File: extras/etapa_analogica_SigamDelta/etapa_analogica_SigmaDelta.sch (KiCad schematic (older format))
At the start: 19 parts, among them P1 CONN_02X10, P2 CONN_01X03, P3 CONN_02X10, P4 BNC

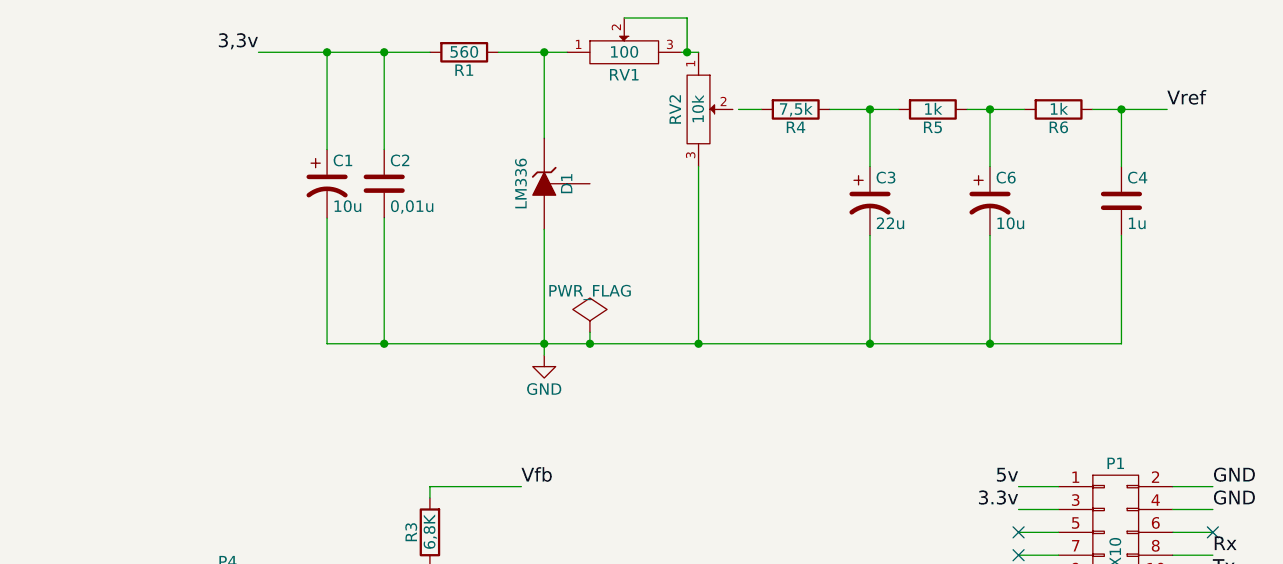
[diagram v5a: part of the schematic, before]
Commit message: choque en filtro vref
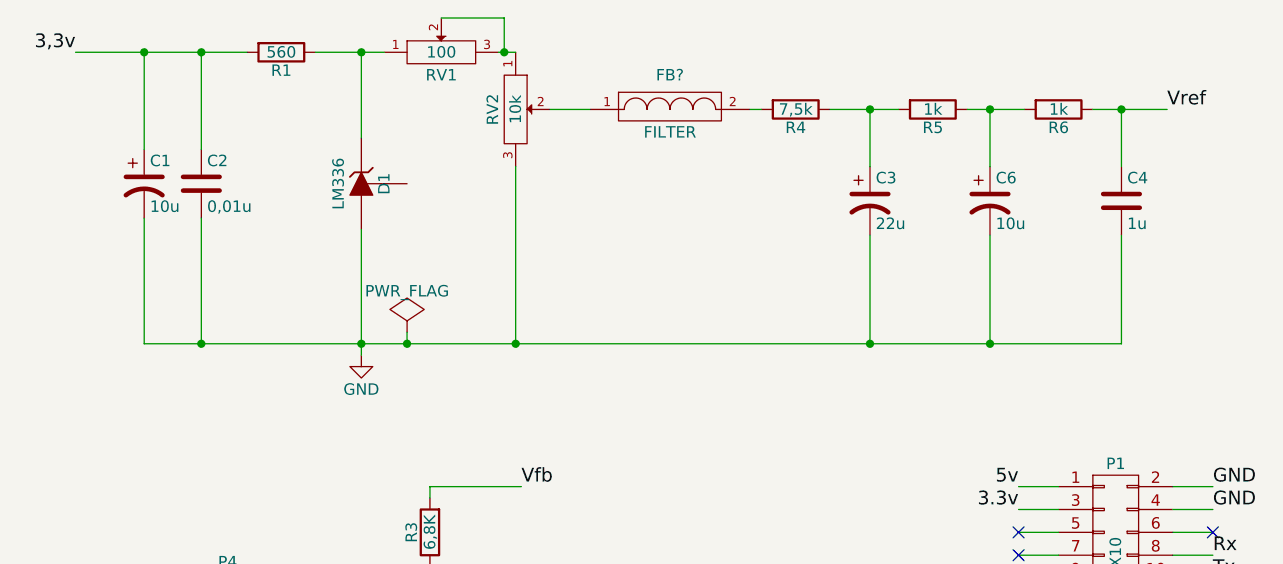
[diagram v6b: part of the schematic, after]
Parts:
- added FB?: FILTER, symbol FILTER
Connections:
- net at RV2.2: now also FB?.1
- net at R4.2: now also FB?.2
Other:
- moved on the sheet: C1, C2, D1, R1, RV1, RV2
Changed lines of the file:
@@
 L C C2
 U 1 1 56153EF9
-P 3800 1825
-F 0 "C2" H 3825 1925 50  0000 L CNN
-F 1 "0,01u" H 3825 1725 50  0000 L CNN
-F 2 "Capacitors_SMD:C_0805" H 3838 1675 30  0001 C CNN
-F 3 "" H 3800 1825 60  0000 C CNN
-	1    3800 1825
+P 3000 1825
+F 0 "C2" H 3025 1925 50  0000 L CNN
+F 1 "0,01u" H 3025 1725 50  0000 L CNN
+F 2 "Capacitors_SMD:C_0805" H 3038 1675 30  0001 C CNN
+F 3 "" H 3000 1825 60  0000 C CNN
+	1    3000 1825
 	1    0    0    -1
 $EndComp
@@
 L R R1
 U 1 1 56153FC2
-P 4150 1250
-F 0 "R1" V 4230 1250 50  0000 C CNN
-F 1 "560" V 4150 1250 50  0000 C CNN
-F 2 "Resistors_SMD:R_0805_HandSoldering" V 4080 1250 30  0001 C CNN
-F 3 "" H 4150 1250 30  0000 C CNN
-	1    4150 1250
+P 3350 1250
+F 0 "R1" V 3430 1250 50  0000 C CNN
+F 1 "560" V 3350 1250 50  0000 C CNN
+F 2 "Resistors_SMD:R_0805_HandSoldering" V 3280 1250 30  0001 C CNN
+F 3 "" H 3350 1250 30  0000 C CNN
+	1    3350 1250
 	0    1    1    0
 $EndComp
@@
 L LM336 D1
 U 1 1 56154941
-P 4900 1825
-F 0 "D1" V 4600 1825 50  0000 C CNN
-F 1 "LM336" V 4400 1825 50  0000 C CNN
-F 2 "LEDs:LED-5MM" V 4500 1825 60  0001 C CNN
-F 3 "" V 4500 1825 60  0000 C CNN
-	1    4900 1825
+P 4100 1825
+F 0 "D1" V 3800 1825 50  0000 C CNN
+F 1 "LM336" V 3600 1825 50  0000 C CNN
+F 2 "LEDs:LED-5MM" V 3700 1825 60  0001 C CNN
+F 3 "" V 3700 1825 60  0000 C CNN
+	1    4100 1825
 	1    0    0    -1
 $EndComp
@@
 L POT RV1
 U 1 1 56154BFA
-P 4850 1250
-F 0 "RV1" H 4850 1150 50  0000 C CNN
-F 1 "100" H 4850 1250 50  0000 C CNN
-F 2 "Potentiometers:Potentiometer_Bourns_3296W_3-8Zoll_Inline_ScrewUp" H 4850 1250 60  0001 C CNN
-F 3 "" H 4850 1250 60  0000 C CNN
-	1    4850 1250
+P 4050 1250
+F 0 "RV1" H 4050 1150 50  0000 C CNN
+F 1 "100" H 4050 1250 50  0000 C CNN
+F 2 "Potentiometers:Potentiometer_Bourns_3296W_3-8Zoll_Inline_ScrewUp" H 4050 1250 60  0001 C CNN
+F 3 "" H 4050 1250 60  0000 C CNN
+	1    4050 1250
 	1    0    0    -1
 $EndComp
@@
 L GND #PWR3
 U 1 1 5615637B
-P 4500 2575
-F 0 "#PWR3" H 4500 2325 50  0001 C CNN
-F 1 "GND" H 4500 2425 50  0000 C CNN
-F 2 "" H 4500 2575 60  0000 C CNN
-F 3 "" H 4500 2575 60  0000 C CNN
-	1    4500 2575
+P 3700 2575
+F 0 "#PWR3" H 3700 2325 50  0001 C CNN
+F 1 "GND" H 3700 2425 50  0000 C CNN
+F 2 "" H 3700 2575 60  0000 C CNN
+F 3 "" H 3700 2575 60  0000 C CNN
+	1    3700 2575
 	1    0    0    -1
 $EndComp
@@
 L POT RV2
 U 1 1 5617E04B
-P 5175 1500
-F 0 "RV2" H 5175 1400 50  0000 C CNN
-F 1 "10k" H 5175 1500 50  0000 C CNN
-F 2 "Potentiometers:Potentiometer_Bourns_3296W_3-8Zoll_Inline_ScrewUp" H 5175 1500 60  0001 C CNN
-F 3 "" H 5175 1500 60  0000 C CNN
-	1    5175 1500
+P 4375 1500
+F 0 "RV2" H 4375 1400 50  0000 C CNN
+F 1 "10k" H 4375 1500 50  0000 C CNN
+F 2 "Potentiometers:Potentiometer_Bourns_3296W_3-8Zoll_Inline_ScrewUp" H 4375 1500 60  0001 C CNN
+F 3 "" H 4375 1500 60  0000 C CNN
+	1    4375 1500
 	0    1    1    0
 $EndComp
@@
 Wire Wire Line
 	7025 1500 7025 1750
-Connection ~ 3800 1250
-Wire Wire Line
-	3800 1250 3800 1675
-Connection ~ 3550 1250
-Connection ~ 4500 2525
-Connection ~ 3800 2525
-Wire Wire Line
-	3550 2525 7025 2525
+Connection ~ 3000 1250
+Wire Wire Line
+	3000 1250 3000 1675
+Connection ~ 2750 1250
+Connection ~ 3700 2525
+Connection ~ 3000 2525
 Wire Wire Line
 	4000 4050 4000 4000
@@
 	7025 2525 7025 2050
 Wire Wire Line
-	4500 2025 4500 2575
-Wire Wire Line
-	3800 1975 3800 2525
-Wire Wire Line
-	3550 2525 3550 1975
+	3700 2025 3700 2575
+Wire Wire Line
+	3000 1975 3000 2525
+Wire Wire Line
+	2750 2525 2750 1975
 Wire Wire Line
 	4000 3200 4000 3150
@@
 	6900 1500 7225 1500
 Wire Wire Line
-	3250 1250 4000 1250
+	2450 1250 3200 1250
 $Comp
 L R R4
@@
 L CP1 C1
 U 1 1 56181DAE
-P 3550 1825
-F 0 "C1" H 3575 1925 50  0000 L CNN
-F 1 "10u" H 3575 1725 50  0000 L CNN
-F 2 "Capacitors_SMD:c_elec_4x5.7" H 3550 1825 60  0001 C CNN
-F 3 "" H 3550 1825 60  0000 C CNN
-	1    3550 1825
-	1    0    0    -1
-$EndComp
-Wire Wire Line
-	3550 1250 3550 1675
+P 2750 1825
+F 0 "C1" H 2775 1925 50  0000 L CNN
+F 1 "10u" H 2775 1725 50  0000 L CNN
+F 2 "Capacitors_SMD:c_elec_4x5.7" H 2750 1825 60  0001 C CNN
+F 3 "" H 2750 1825 60  0000 C CNN
+	1    2750 1825
+	1    0    0    -1
+$EndComp
+Wire Wire Line
+	2750 1250 2750 1675
 $Comp
 L CONN_02X10 P3
@@
 	1    0    0    -1
 $EndComp
-Wire Wire Line
-	5350 1500 5450 1500
 Wire Wire Line
 	9300 3450 9475 3450
@@
 Text Label 4400 3600 0    60   ~ 0
 Vin
-Text Label 3250 1250 2    60   ~ 0
+Text Label 2450 1250 2    60   ~ 0
 3,3v
 Text Label 7225 1500 0    60   ~ 0
@@
 L PWR_FLAG #FLG1
 U 1 1 561CAC5A
-P 4700 2475
-F 0 "#FLG1" H 4700 2570 50  0001 C CNN
-F 1 "PWR_FLAG" H 4700 2655 50  0000 C CNN
-F 2 "" H 4700 2475 60  0000 C CNN
-F 3 "" H 4700 2475 60  0000 C CNN
-	1    4700 2475
-	1    0    0    -1
-$EndComp
-Wire Wire Line
-	4700 2475 4700 2525
-Connection ~ 4700 2525
-Wire Wire Line
-	5100 1250 5175 1250
-Wire Wire Line
-	5175 1750 5175 2525
-Connection ~ 5175 2525
-Wire Wire Line
-	4300 1250 4600 1250
-Wire Wire Line
-	4500 1625 4500 1250
-Connection ~ 4500 1250
-Wire Wire Line
-	4850 1100 5125 1100
-Wire Wire Line
-	5125 1100 5125 1250
-Connection ~ 5125 1250
+P 3900 2475
+F 0 "#FLG1" H 3900 2570 50  0001 C CNN
+F 1 "PWR_FLAG" H 3900 2655 50  0000 C CNN
+F 2 "" H 3900 2475 60  0000 C CNN
+F 3 "" H 3900 2475 60  0000 C CNN
+	1    3900 2475
+	1    0    0    -1
+$EndComp
+Wire Wire Line
+	3900 2475 3900 2525
+Connection ~ 3900 2525
+Wire Wire Line
+	4300 1250 4375 1250
+Wire Wire Line
+	4375 1750 4375 2525
+Connection ~ 4375 2525
+Wire Wire Line
+	3500 1250 3800 1250
+Wire Wire Line
+	3700 1625 3700 1250
+Connection ~ 3700 1250
+Wire Wire Line
+	4050 1100 4325 1100
+Wire Wire Line
+	4325 1100 4325 1250
+Connection ~ 4325 1250
 $Comp
 L R R5
@@
 	0    1    1    0
 $EndComp
+$Comp
+L FILTER FB?
+U 1 1 561C7944
+P 5050 1500
+F 0 "FB?" H 5050 1650 50  0000 C CNN
+F 1 "FILTER" H 5050 1400 50  0000 C CNN
+F 2 "" H 5050 1500 60  0000 C CNN
+F 3 "" H 5050 1500 60  0000 C CNN
+	1    5050 1500
+	1    0    0    -1
+$EndComp
+Wire Wire Line
+	5400 1500 5450 1500
+Wire Wire Line
+	4700 1500 4525 1500
+Wire Wire Line
+	7025 2525 2750 2525
 $EndSCHEMATC

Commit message: chasis bnc
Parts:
- FB1: renamed from FB?; footprint (none) -> Capacitors_SMD:C_0805_HandSoldering
- P1, P3: footprint (none) -> Pin_Headers:Pin_Header_Straight_2x10
- P2: footprint (none) -> Pin_Headers:Pin_Header_Straight_1x03
- P4: footprint (none) -> chasis_bnc:chasis_bnc
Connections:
- net Rx: now also P1.14 (P14); no longer P1.8 (P8)
- net Tx: now also P1.12 (P12); no longer P1.10 (P10)
- no-connect marks 27 -> 28
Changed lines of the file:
@@
 $EndComp
 $Comp
-L GND #PWR3
+L GND #PWR01
 U 1 1 5615637B
 P 3700 2575
-F 0 "#PWR3" H 3700 2325 50  0001 C CNN
+F 0 "#PWR01" H 3700 2325 50  0001 C CNN
 F 1 "GND" H 3700 2425 50  0000 C CNN
 F 2 "" H 3700 2575 60  0000 C CNN
@@
 $EndComp
 $Comp
-L GND #PWR2
+L GND #PWR02
 U 1 1 561564F5
 P 4000 4050
-F 0 "#PWR2" H 4000 3800 50  0001 C CNN
+F 0 "#PWR02" H 4000 3800 50  0001 C CNN
 F 1 "GND" H 4000 3900 50  0000 C CNN
 F 2 "" H 4000 4050 60  0000 C CNN
@@
 F 0 "P3" H 9050 4050 50  0000 C CNN
 F 1 "CONN_02X10" V 9050 3500 50  0000 C CNN
-F 2 "" H 9050 2300 60  0000 C CNN
+F 2 "Pin_Headers:Pin_Header_Straight_2x10" H 9050 2300 60  0001 C CNN
 F 3 "" H 9050 2300 60  0000 C CNN
 	1    9050 3500
@@
 F 0 "P1" H 7000 4150 50  0000 C CNN
 F 1 "CONN_02X10" V 7000 3600 50  0000 C CNN
-F 2 "" H 7000 2400 60  0000 C CNN
+F 2 "Pin_Headers:Pin_Header_Straight_2x10" H 7000 2400 60  0001 C CNN
 F 3 "" H 7000 2400 60  0000 C CNN
 	1    7000 3600
@@
 NoConn ~ 7425 3950
 NoConn ~ 7425 3850
-Text Label 7425 3450 0    60   ~ 0
+Text Label 7425 3750 0    60   ~ 0
 Rx
-Text Label 7425 3550 0    60   ~ 0
+Text Label 7425 3650 0    60   ~ 0
 Tx
-NoConn ~ 7425 3750
-NoConn ~ 7425 3650
+NoConn ~ 7425 3450
+NoConn ~ 7425 3550
 $Comp
 L CONN_01X03 P2
@@
 F 0 "P2" H 8900 2500 50  0000 C CNN
 F 1 "CONN_01X03" V 9000 2300 50  0000 C CNN
-F 2 "" H 8900 2300 60  0000 C CNN
+F 2 "Pin_Headers:Pin_Header_Straight_1x03" H 8900 2300 60  0001 C CNN
 F 3 "" H 8900 2300 60  0000 C CNN
 	1    8900 2300
@@
 F 0 "P4" H 3135 3720 50  0000 C CNN
 F 1 "BNC" V 3235 3540 50  0000 C CNN
-F 2 "" H 3125 3600 60  0000 C CNN
+F 2 "chasis_bnc:chasis_bnc" H 3125 3600 60  0001 C CNN
 F 3 "" H 3125 3600 60  0000 C CNN
 	1    3125 3600
@@
 $EndComp
 $Comp
-L GND #PWR1
+L GND #PWR03
 U 1 1 561CA0F5
 P 3125 3925
-F 0 "#PWR1" H 3125 3675 50  0001 C CNN
+F 0 "#PWR03" H 3125 3675 50  0001 C CNN
 F 1 "GND" H 3125 3775 50  0000 C CNN
 F 2 "" H 3125 3925 60  0000 C CNN
@@
 	3125 3925 3125 3800
 $Comp
-L GND #PWR4
+L GND #PWR04
 U 1 1 561CA2C4
 P 8575 2500
-F 0 "#PWR4" H 8575 2250 50  0001 C CNN
+F 0 "#PWR04" H 8575 2250 50  0001 C CNN
 F 1 "GND" H 8575 2350 50  0000 C CNN
 F 2 "" H 8575 2500 60  0000 C CNN
@@
 Connection ~ 8575 2400
 $Comp
-L PWR_FLAG #FLG1
+L PWR_FLAG #FLG05
 U 1 1 561CAC5A
 P 3900 2475
-F 0 "#FLG1" H 3900 2570 50  0001 C CNN
+F 0 "#FLG05" H 3900 2570 50  0001 C CNN
 F 1 "PWR_FLAG" H 3900 2655 50  0000 C CNN
 F 2 "" H 3900 2475 60  0000 C CNN
@@
 $EndComp
 $Comp
-L FILTER FB?
+L FILTER FB1
 U 1 1 561C7944
 P 5050 1500
-F 0 "FB?" H 5050 1650 50  0000 C CNN
+F 0 "FB1" H 5050 1650 50  0000 C CNN
 F 1 "FILTER" H 5050 1400 50  0000 C CNN
-F 2 "" H 5050 1500 60  0000 C CNN
+F 2 "Capacitors_SMD:C_0805_HandSoldering" H 5050 1500 60  0001 C CNN
 F 3 "" H 5050 1500 60  0000 C CNN
 	1    5050 1500
@@
 Wire Wire Line
 	7025 2525 2750 2525
+NoConn ~ 3900 1825
 $EndSCHEMATC

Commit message: Cambiados capacitores filtro Vref por 10uF tantalio. Falta cambiar electrolítico de entrada.
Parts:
- removed C4: 1u, Capacitors_SMD:C_0805, symbol C
- added C?: 10u, Capacitors_Tantalum_SMD:TantalC_SizeA_EIA-3216_HandSoldering, symbol CP1
- C3: value 22u -> 10u; footprint Capacitors_SMD:c_elec_4x5.7 -> Capacitors_Tantalum_SMD:TantalC_SizeA_EIA-3216_HandSoldering
- D1: symbol LM336 -> LM336-RESCUE-etapa_analogica_SigmaDelta
- R4: value 7,5k -> 15k
- R5, R6: value 1k -> 15k
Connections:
- net GND: now also C?.2
- net N40: now also C?.1
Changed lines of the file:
@@
 EESchema Schematic File Version 2
+LIBS:etapa_analogica_SigmaDelta-rescue
 LIBS:power
 LIBS:device
@@
 $EndComp
 $Comp
-L LM336 D1
+L LM336-RESCUE-etapa_analogica_SigmaDelta D1
 U 1 1 56154941
 P 4100 1825
@@
 F 3 "" H 4050 1250 60  0000 C CNN
 	1    4050 1250
-	1    0    0    -1
-$EndComp
-$Comp
-L C C4
-U 1 1 56154D38
-P 7025 1900
-F 0 "C4" H 7050 2000 50  0000 L CNN
-F 1 "1u" H 7050 1800 50  0000 L CNN
-F 2 "Capacitors_SMD:C_0805" H 7063 1750 30  0001 C CNN
-F 3 "" H 7025 1900 60  0000 C CNN
-	1    7025 1900
 	1    0    0    -1
 $EndComp
@@
 P 5925 1900
 F 0 "C3" H 5950 2000 50  0000 L CNN
-F 1 "22u" H 5950 1800 50  0000 L CNN
-F 2 "Capacitors_SMD:c_elec_4x5.7" H 5925 1900 60  0001 C CNN
+F 1 "10u" H 5950 1800 50  0000 L CNN
+F 2 "Capacitors_Tantalum_SMD:TantalC_SizeA_EIA-3216_HandSoldering" H 5925 1900 60  0001 C CNN
 F 3 "" H 5925 1900 60  0000 C CNN
 	1    5925 1900
@@
 	4000 4050 4000 4000
 Wire Wire Line
-	7025 2525 7025 2050
-Wire Wire Line
 	3700 2025 3700 2575
 Wire Wire Line
@@
 P 5600 1500
 F 0 "R4" V 5680 1500 50  0000 C CNN
-F 1 "7,5k" V 5600 1500 50  0000 C CNN
+F 1 "15k" V 5600 1500 50  0000 C CNN
 F 2 "Resistors_SMD:R_0805_HandSoldering" V 5530 1500 30  0001 C CNN
 F 3 "" H 5600 1500 30  0000 C CNN
@@
 P 6200 1500
 F 0 "R5" V 6280 1500 50  0000 C CNN
-F 1 "1k" V 6200 1500 50  0000 C CNN
+F 1 "15k" V 6200 1500 50  0000 C CNN
 F 2 "Resistors_SMD:R_0805_HandSoldering" V 6130 1500 30  0001 C CNN
 F 3 "" H 6200 1500 30  0000 C CNN
@@
 P 6750 1500
 F 0 "R6" V 6830 1500 50  0000 C CNN
-F 1 "1k" V 6750 1500 50  0000 C CNN
+F 1 "15k" V 6750 1500 50  0000 C CNN
 F 2 "Resistors_SMD:R_0805_HandSoldering" V 6680 1500 30  0001 C CNN
 F 3 "" H 6750 1500 30  0000 C CNN
@@
 	7025 2525 2750 2525
 NoConn ~ 3900 1825
+$Comp
+L CP1 C?
+U 1 1 56200ADB
+P 7025 1900
+F 0 "C?" H 7050 2000 50  0000 L CNN
+F 1 "10u" H 7050 1800 50  0000 L CNN
+F 2 "Capacitors_Tantalum_SMD:TantalC_SizeA_EIA-3216_HandSoldering" H 7025 1900 60  0001 C CNN
+F 3 "" H 7025 1900 60  0000 C CNN
+	1    7025 1900
+	1    0    0    -1
+$EndComp
+Wire Wire Line
+	7025 2050 7025 2525
 $EndSCHEMATC
